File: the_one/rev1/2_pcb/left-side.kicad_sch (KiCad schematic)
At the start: 39 parts, among them SW1 KeySwitch, SW10 KeySwitch, SW11 KeySwitch, SW12 KeySwitch, SW13 KeySwitch, SW14 KeySwitch, SW15 KeySwitch, SW16 KeySwitch, SW17 KeySwitch, SW18 KeySwitch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

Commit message: update KiCAD schematcis
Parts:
- U1: footprint RPi_Pico:RPi_Pico_SMD_TH -> MCU_RaspberryPi_and_Boards:RPi_Pico_SMD_TH
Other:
- moved on the sheet: D1, D10, D11, D12, D13, D14, D15, D16, D17, D18, D19, D2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

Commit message: update rev1 README
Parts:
- U1: value Pico -> RP2040
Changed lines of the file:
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@@
 			)
 		)
-		(property "Value" "Pico"
+		(property "Value" "RP2040"
 			(at 223.52 39.37 0)
 			(show_name no)

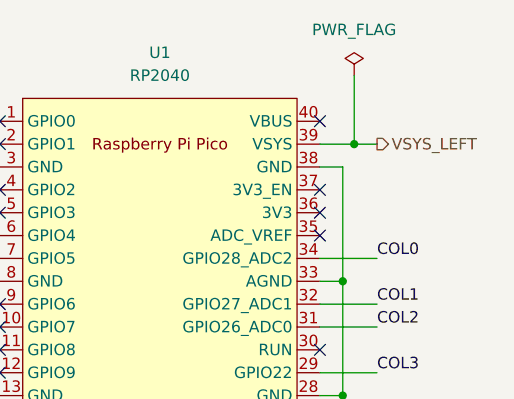
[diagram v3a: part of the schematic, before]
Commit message: change power supply pins of rp2040 from VSYS to VBUS
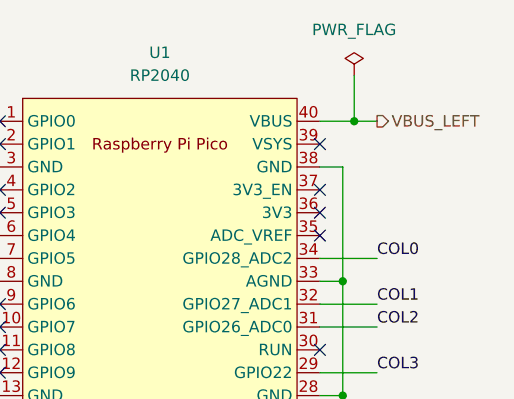
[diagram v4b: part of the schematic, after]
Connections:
- net VBUS_LEFT: now reaches U1.40 (VBUS)
- net VSYS_LEFT: no longer names the net of U1.39 (VSYS)
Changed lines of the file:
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@@
+	)
+	(junction
+		(at 245.11 44.45)
+		(diameter 0)
+		(color 0 0 0 0)
 	)
 	(junction
@@
 	)
 	(junction
-		(at 245.11 46.99)
-		(diameter 0)
-		(color 0 0 0 0)
-	)
-	(junction
 		(at 80.01 114.3)
 		(diameter 0)
@@
 	)
 	(no_connect
+		(at 241.3 46.99)
+	)
+	(no_connect
 		(at 241.3 69.85)
 	)
@@
 		(at 205.74 92.71)
 	)
-	(no_connect
-		(at 241.3 44.45)
-	)
 	(wire
 		(pts
@@
 	(wire
 		(pts
-			(xy 245.11 46.99) (xy 247.65 46.99)
+			(xy 245.11 44.45) (xy 247.65 44.45)
 		)
 		(stroke
@@
 	(wire
 		(pts
+			(xy 241.3 44.45) (xy 245.11 44.45)
+		)
+		(stroke
+			(width 0)
+			(type default)
+		)
+	)
+	(wire
+		(pts
 			(xy 241.3 77.47) (xy 247.65 77.47)
 		)
@@
 	(wire
 		(pts
-			(xy 241.3 46.99) (xy 245.11 46.99)
-		)
-		(stroke
-			(width 0)
-			(type default)
-		)
-	)
-	(wire
-		(pts
 			(xy 199.39 49.53) (xy 199.39 62.23)
 		)
@@
 	(wire
 		(pts
-			(xy 245.11 39.37) (xy 245.11 46.99)
+			(xy 245.11 39.37) (xy 245.11 44.45)
 		)
 		(stroke
@@
 		)
 	)
-	(hierarchical_label "VSYS_LEFT"
+	(hierarchical_label "VBUS_LEFT"
 		(shape output)
-		(at 247.65 46.99 0)
-		(effects
-			(font
+		(at 247.65 44.45 0)
+		(effects
+			(font

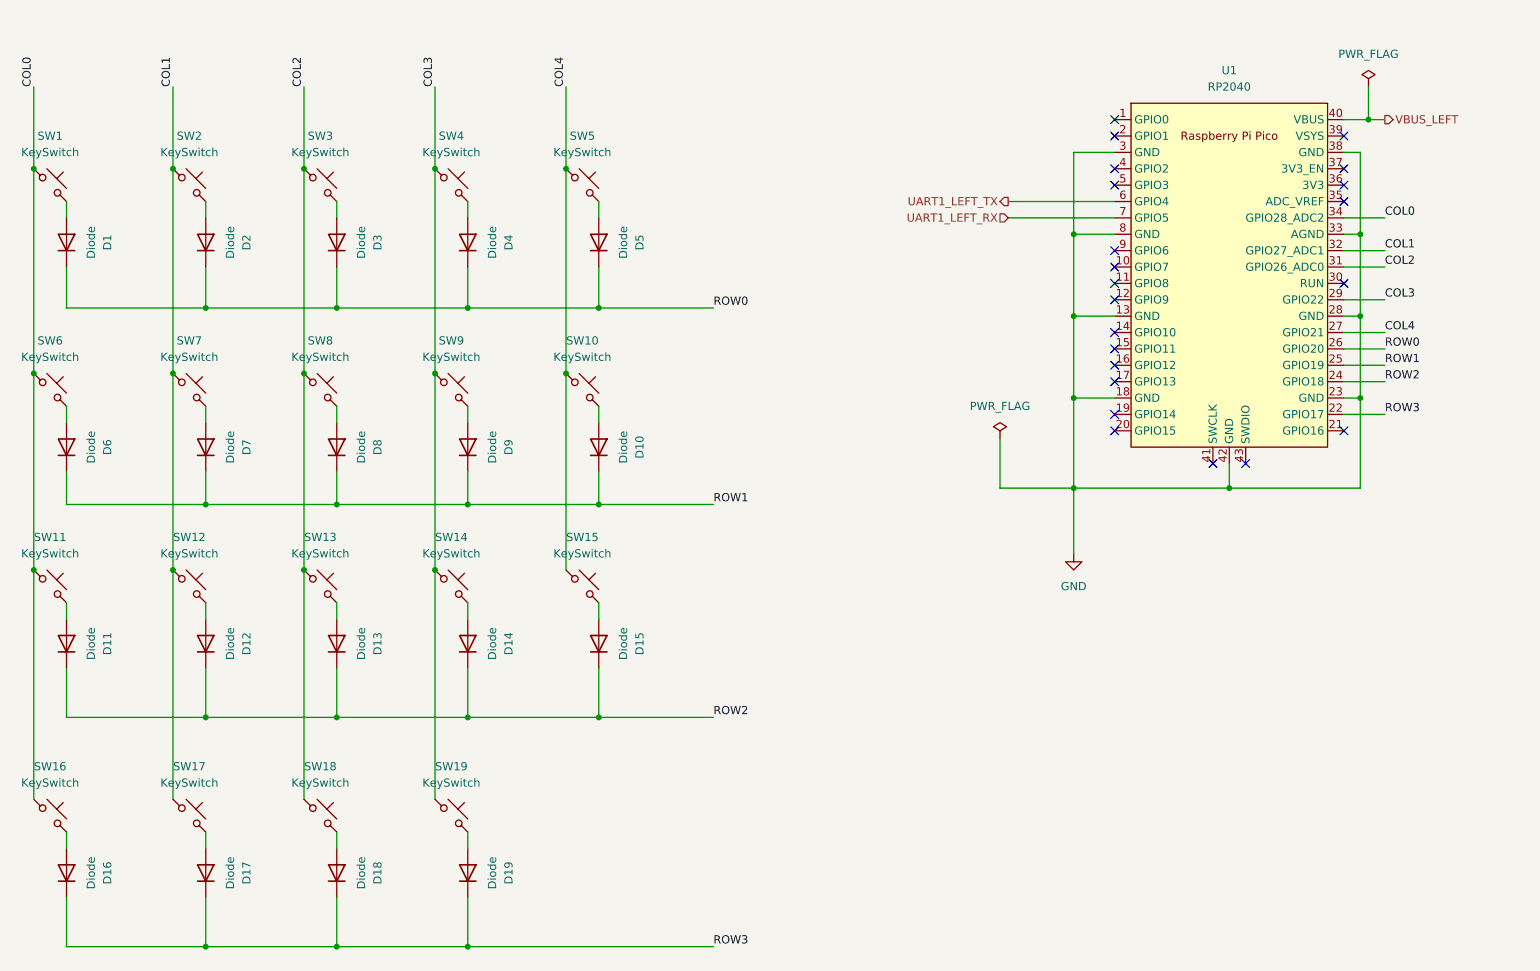
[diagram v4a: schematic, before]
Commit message: add TRRS jacks into the schematics
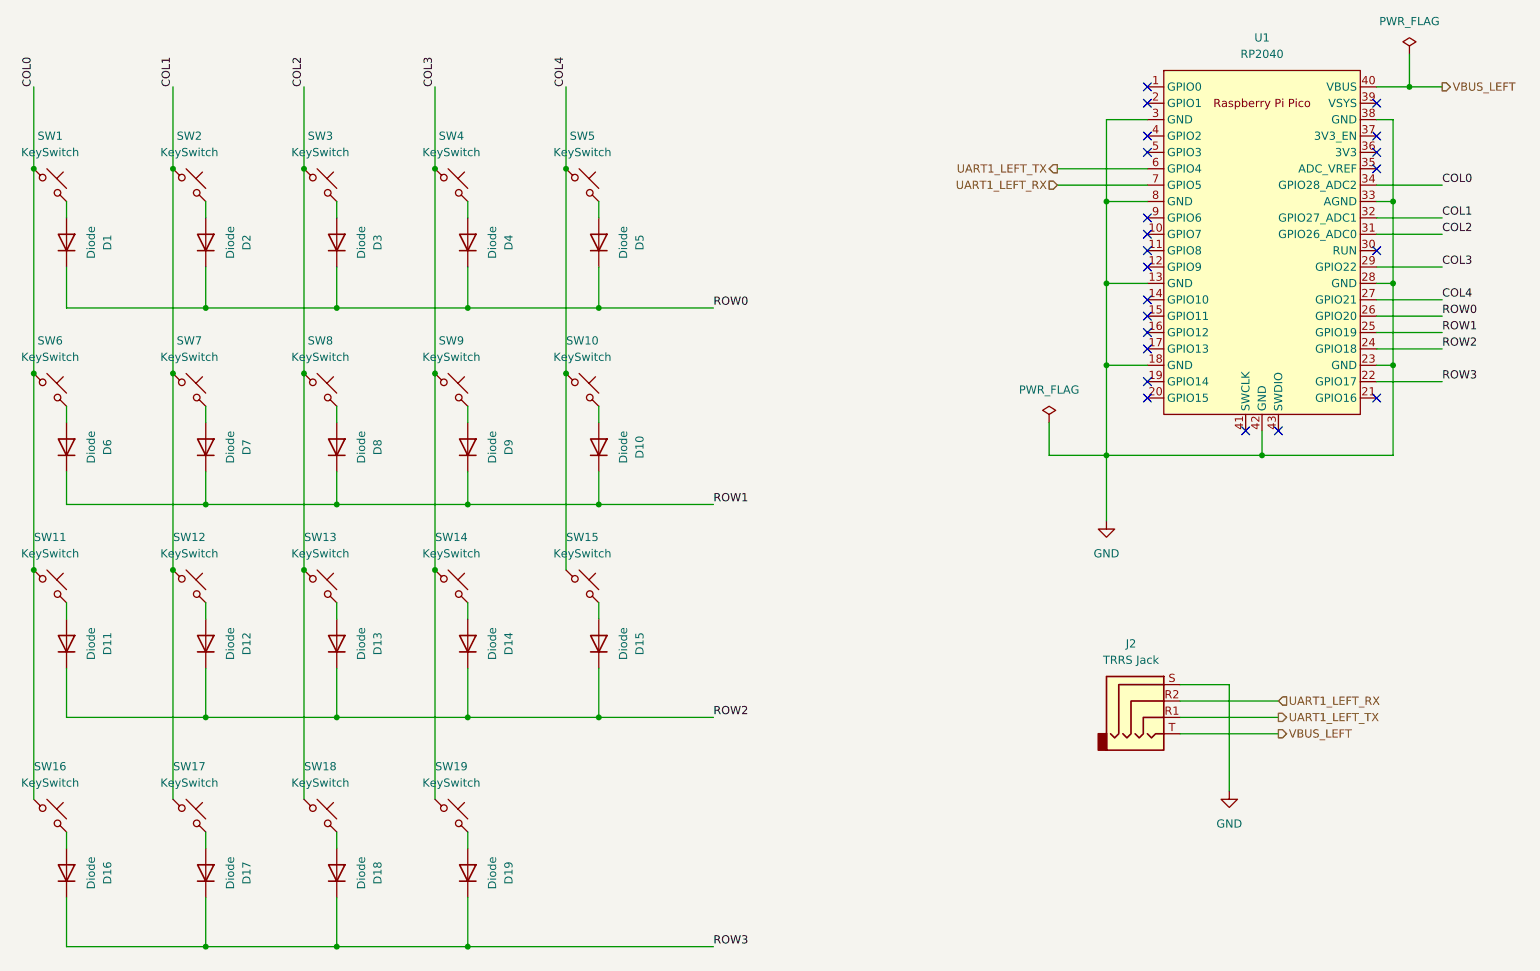
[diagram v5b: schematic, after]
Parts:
- added J2: TRRS Jack, symbol Connector_Audio:AudioJack4
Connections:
- net GND: now also J2.S
- net UART1_LEFT_RX: now also J2.R2
- net UART1_LEFT_TX: now also J2.R1
- net VBUS_LEFT: now also J2.T
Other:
- moved on the sheet: U1
